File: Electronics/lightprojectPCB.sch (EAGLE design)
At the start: 12 parts, among them IC1 7805T

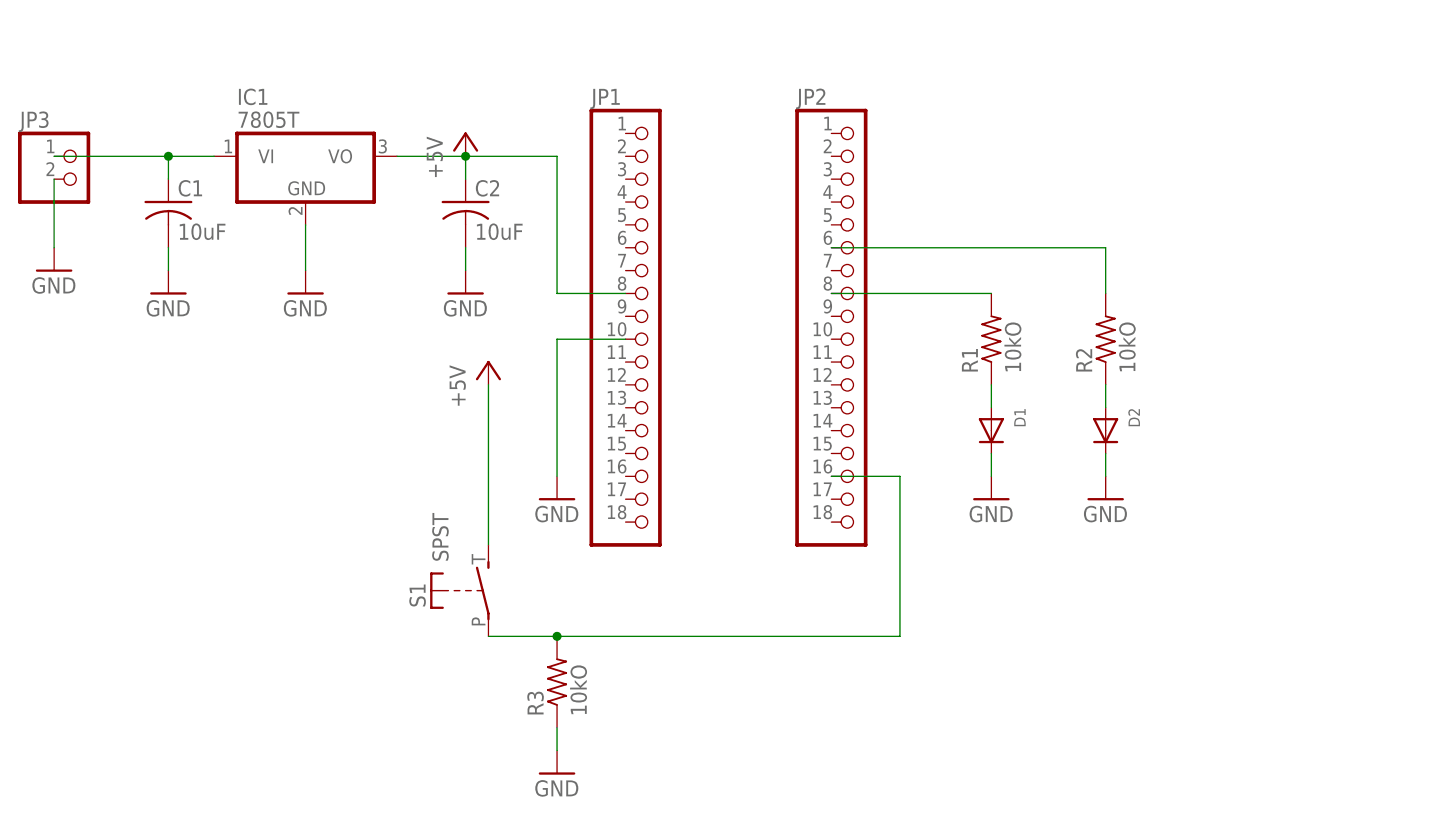
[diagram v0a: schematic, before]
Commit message: Add files via upload
Updated schematic with Arduino footprint
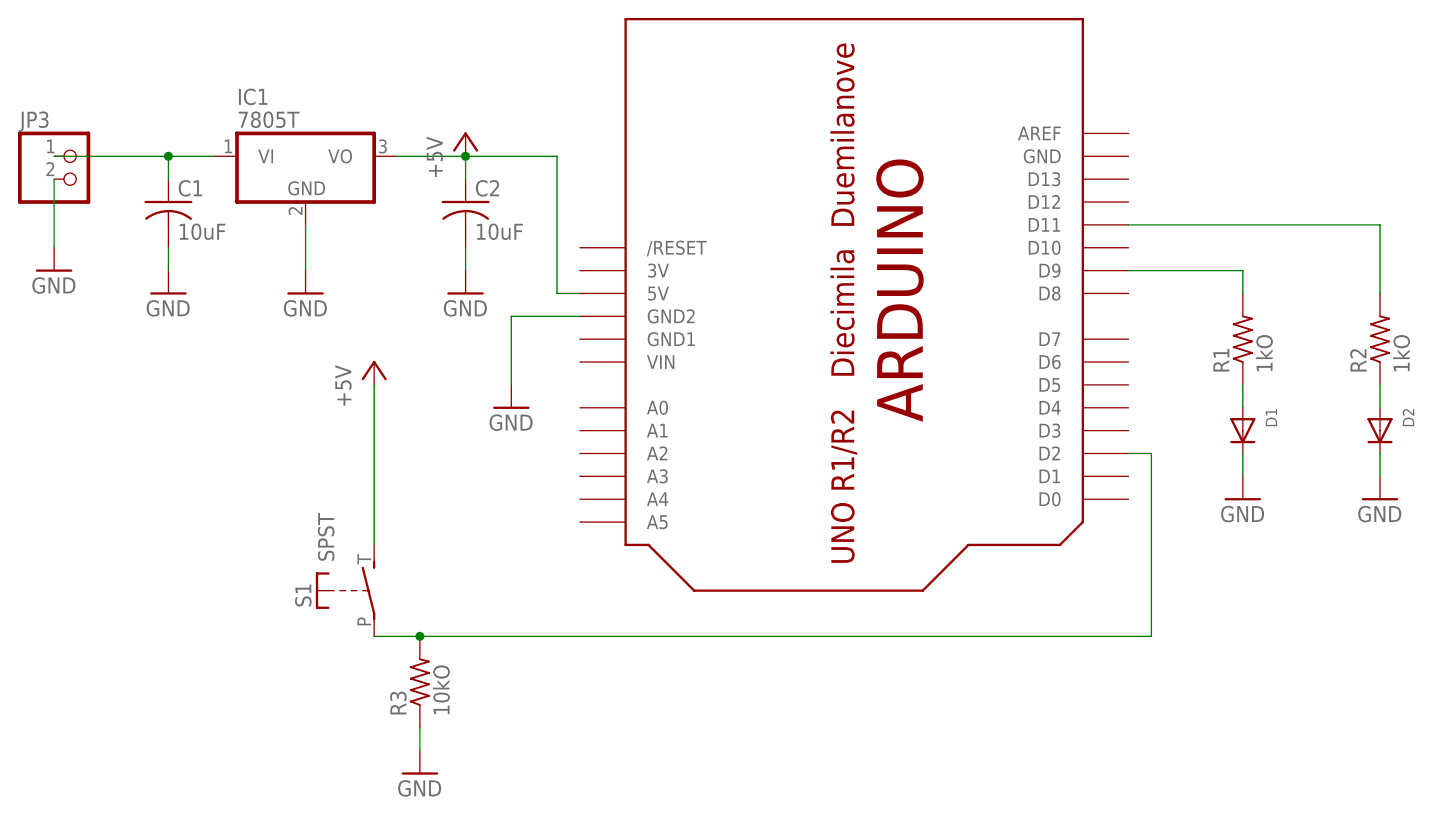
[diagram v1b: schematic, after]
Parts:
- removed JP1, JP2: (no value), adafruit:PINHD-1X18
- added U$1: ARDUINO-BPLACE, adafruit:ARDUINO-BPLACE
- R1, R2: value 10kO -> 1kO
- R3: device adafruit:R-US_FLIPFLOP -> adafruit:R-US_M0805
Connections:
- net +5V: now also U$1.5V; no longer JP1.8
- net GND: now also U$1.GND2; no longer JP1.10
- net N$1: now also R1.2, U$1.D9; no longer JP2.16, R3.2, S1.P
- net N$5: now also R3.2, S1.P, U$1.D2; no longer JP2.8, R1.2
- net N$6: now also U$1.D11; no longer JP2.6
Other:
- moved on the sheet: D1, D2, R1, R2, R3, S1

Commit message: Add files via upload
Updated schematic and board to include an analog read of the battery voltage - still need to address polygon pour and make sure there are appropriate components in the lab for my design
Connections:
- net +5V: now also U$1.A1
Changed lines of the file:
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@@
 <attribute name="VALUE" x="-5.08" y="71.12" size="1.778" layer="96"/>
 </instance>
-<instance part="GND8" gate="1" x="48.26" y="58.42">
-<attribute name="VALUE" x="45.72" y="55.88" size="1.778" layer="96"/>
+<instance part="GND8" gate="1" x="50.8" y="66.04">
+<attribute name="VALUE" x="48.26" y="63.5" size="1.778" layer="96"/>
 </instance>
 <instance part="R3" gate="G$1" x="38.1" y="27.94" rot="R90">
@@
 <segment>
 <pinref part="GND8" gate="1" pin="GND"/>
-<wire x1="48.26" y1="60.96" x2="48.26" y2="68.58" width="0.1524" layer="91"/>
 <pinref part="U$1" gate="G$1" pin="GND2"/>
-<wire x1="48.26" y1="68.58" x2="55.88" y2="68.58" width="0.1524" layer="91"/>
+<wire x1="50.8" y1="68.58" x2="55.88" y2="68.58" width="0.1524" layer="91"/>
 </segment>
 </net>
@@
 <pinref part="P+2" gate="1" pin="+5V"/>
 <pinref part="S1" gate="G$1" pin="S"/>
-<wire x1="33.02" y1="60.96" x2="33.02" y2="43.18" width="0.1524" layer="91"/>
+<wire x1="33.02" y1="60.96" x2="33.02" y2="55.88" width="0.1524" layer="91"/>
+<pinref part="U$1" gate="G$1" pin="A1"/>
+<wire x1="33.02" y1="55.88" x2="33.02" y2="43.18" width="0.1524" layer="91"/>
+<wire x1="55.88" y1="55.88" x2="33.02" y2="55.88" width="0.1524" layer="91"/>
+<junction x="33.02" y="55.88"/>
 </segment>
 </net>
